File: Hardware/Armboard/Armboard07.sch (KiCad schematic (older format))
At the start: 30 parts

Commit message: Assigned R/L/C footprints
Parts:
- R24, R25, R26, R27, R28, R29, R30, R31, R32, R33: renamed from R?; footprint (none) -> Resistor_SMD:R_0603_1608Metric_Pad1.05x0.95mm_HandSolder
- gave numbers to parts that had none: 20

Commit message: Added more footprints
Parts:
- Conn14, Conn15, Conn16, Conn17: footprint (none) -> MRDT_Connectors:MOLEX_SL_02_Horizontal
- D18, D19, D20, D21, D22, D23, D24, D25, D26, D27: footprint (none) -> LED_SMD:LED_0603_1608Metric_Pad1.05x0.95mm_HandSolder
- SW1, SW2, SW3, SW4, SW5, SW6: footprint (none) -> Button_Switch_SMD:SW_Push_1P1T_NO_6x6mm_H9.5mm
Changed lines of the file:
@@
 F 0 "D24" V 6989 2892 50  0000 R CNN
 F 1 "LED" V 6898 2892 50  0000 R CNN
-F 2 "" H 6950 3010 50  0001 C CNN
+F 2 "LED_SMD:LED_0603_1608Metric_Pad1.05x0.95mm_HandSolder" H 6950 3010 50  0001 C CNN
 F 3 "~" H 6950 3010 50  0001 C CNN
 	1    6950 3010
@@
 F 0 "Conn14" H 7418 2618 60  0000 L CNN
 F 1 "Molex_SL_02" H 7418 2512 60  0000 L CNN
-F 2 "" H 7290 2360 60  0001 C CNN
+F 2 "MRDT_Connectors:MOLEX_SL_02_Horizontal" H 7290 2360 60  0001 C CNN
 F 3 "" H 7290 2360 60  0001 C CNN
 	1    7290 2460
@@
 F 0 "D25" V 6989 4792 50  0000 R CNN
 F 1 "LED" V 6898 4792 50  0000 R CNN
-F 2 "" H 6950 4910 50  0001 C CNN
+F 2 "LED_SMD:LED_0603_1608Metric_Pad1.05x0.95mm_HandSolder" H 6950 4910 50  0001 C CNN
 F 3 "~" H 6950 4910 50  0001 C CNN
 	1    6950 4910
@@
 F 0 "Conn15" H 7418 4518 60  0000 L CNN
 F 1 "Molex_SL_02" H 7418 4412 60  0000 L CNN
-F 2 "" H 7290 4260 60  0001 C CNN
+F 2 "MRDT_Connectors:MOLEX_SL_02_Horizontal" H 7290 4260 60  0001 C CNN
 F 3 "" H 7290 4260 60  0001 C CNN
 	1    7290 4360
@@
 F 0 "D26" V 8949 2922 50  0000 R CNN
 F 1 "LED" V 8858 2922 50  0000 R CNN
-F 2 "" H 8910 3040 50  0001 C CNN
+F 2 "LED_SMD:LED_0603_1608Metric_Pad1.05x0.95mm_HandSolder" H 8910 3040 50  0001 C CNN
 F 3 "~" H 8910 3040 50  0001 C CNN
 	1    8910 3040
@@
 F 0 "Conn16" H 9378 2648 60  0000 L CNN
 F 1 "Molex_SL_02" H 9378 2542 60  0000 L CNN
-F 2 "" H 9250 2390 60  0001 C CNN
+F 2 "MRDT_Connectors:MOLEX_SL_02_Horizontal" H 9250 2390 60  0001 C CNN
 F 3 "" H 9250 2390 60  0001 C CNN
 	1    9250 2490
@@
 F 0 "D27" V 8949 4822 50  0000 R CNN
 F 1 "LED" V 8858 4822 50  0000 R CNN
-F 2 "" H 8910 4940 50  0001 C CNN
+F 2 "LED_SMD:LED_0603_1608Metric_Pad1.05x0.95mm_HandSolder" H 8910 4940 50  0001 C CNN
 F 3 "~" H 8910 4940 50  0001 C CNN
 	1    8910 4940
@@
 F 0 "Conn17" H 9378 4548 60  0000 L CNN
 F 1 "Molex_SL_02" H 9378 4442 60  0000 L CNN
-F 2 "" H 9250 4290 60  0001 C CNN
+F 2 "MRDT_Connectors:MOLEX_SL_02_Horizontal" H 9250 4290 60  0001 C CNN
 F 3 "" H 9250 4290 60  0001 C CNN
 	1    9250 4390
@@
 F 0 "SW1" H 2550 2035 50  0000 C CNN
 F 1 "SW_Push" H 2550 1944 50  0000 C CNN
-F 2 "" H 2550 1950 50  0001 C CNN
+F 2 "Button_Switch_SMD:SW_Push_1P1T_NO_6x6mm_H9.5mm" H 2550 1950 50  0001 C CNN
 F 3 "~" H 2550 1950 50  0001 C CNN
 	1    2550 1750
@@
 F 0 "SW2" H 2550 2985 50  0000 C CNN
 F 1 "SW_Push" H 2550 2894 50  0000 C CNN
-F 2 "" H 2550 2900 50  0001 C CNN
+F 2 "Button_Switch_SMD:SW_Push_1P1T_NO_6x6mm_H9.5mm" H 2550 2900 50  0001 C CNN
 F 3 "~" H 2550 2900 50  0001 C CNN
 	1    2550 2700
@@
 F 0 "SW3" H 2550 3935 50  0000 C CNN
 F 1 "SW_Push" H 2550 3844 50  0000 C CNN
-F 2 "" H 2550 3850 50  0001 C CNN
+F 2 "Button_Switch_SMD:SW_Push_1P1T_NO_6x6mm_H9.5mm" H 2550 3850 50  0001 C CNN
 F 3 "~" H 2550 3850 50  0001 C CNN
 	1    2550 3650
@@
 F 0 "SW4" H 2550 4935 50  0000 C CNN
 F 1 "SW_Push" H 2550 4844 50  0000 C CNN
-F 2 "" H 2550 4850 50  0001 C CNN
+F 2 "Button_Switch_SMD:SW_Push_1P1T_NO_6x6mm_H9.5mm" H 2550 4850 50  0001 C CNN
 F 3 "~" H 2550 4850 50  0001 C CNN
 	1    2550 4650
@@
 F 0 "SW5" H 2550 5885 50  0000 C CNN
 F 1 "SW_Push" H 2550 5794 50  0000 C CNN
-F 2 "" H 2550 5800 50  0001 C CNN
+F 2 "Button_Switch_SMD:SW_Push_1P1T_NO_6x6mm_H9.5mm" H 2550 5800 50  0001 C CNN
 F 3 "~" H 2550 5800 50  0001 C CNN
 	1    2550 5600
@@
 F 0 "SW6" H 2550 6835 50  0000 C CNN
 F 1 "SW_Push" H 2550 6744 50  0000 C CNN
-F 2 "" H 2550 6750 50  0001 C CNN
+F 2 "Button_Switch_SMD:SW_Push_1P1T_NO_6x6mm_H9.5mm" H 2550 6750 50  0001 C CNN
 F 3 "~" H 2550 6750 50  0001 C CNN
 	1    2550 6550
@@
 F 0 "D18" H 3493 1495 50  0000 C CNN
 F 1 "LED" H 3493 1586 50  0000 C CNN
-F 2 "" H 3500 1750 50  0001 C CNN
+F 2 "LED_SMD:LED_0603_1608Metric_Pad1.05x0.95mm_HandSolder" H 3500 1750 50  0001 C CNN
 F 3 "~" H 3500 1750 50  0001 C CNN
 	1    3500 1750
@@
 F 0 "D19" H 3493 2445 50  0000 C CNN
 F 1 "LED" H 3493 2536 50  0000 C CNN
-F 2 "" H 3500 2700 50  0001 C CNN
+F 2 "LED_SMD:LED_0603_1608Metric_Pad1.05x0.95mm_HandSolder" H 3500 2700 50  0001 C CNN
 F 3 "~" H 3500 2700 50  0001 C CNN
 	1    3500 2700
@@
 F 0 "D20" H 3493 3395 50  0000 C CNN
 F 1 "LED" H 3493 3486 50  0000 C CNN
-F 2 "" H 3500 3650 50  0001 C CNN
+F 2 "LED_SMD:LED_0603_1608Metric_Pad1.05x0.95mm_HandSolder" H 3500 3650 50  0001 C CNN
 F 3 "~" H 3500 3650 50  0001 C CNN
 	1    3500 3650
@@
 F 0 "D21" H 3493 4395 50  0000 C CNN
 F 1 "LED" H 3493 4486 50  0000 C CNN
-F 2 "" H 3500 4650 50  0001 C CNN
+F 2 "LED_SMD:LED_0603_1608Metric_Pad1.05x0.95mm_HandSolder" H 3500 4650 50  0001 C CNN
 F 3 "~" H 3500 4650 50  0001 C CNN
 	1    3500 4650
@@
 F 0 "D22" H 3493 5345 50  0000 C CNN
 F 1 "LED" H 3493 5436 50  0000 C CNN
-F 2 "" H 3500 5600 50  0001 C CNN
+F 2 "LED_SMD:LED_0603_1608Metric_Pad1.05x0.95mm_HandSolder" H 3500 5600 50  0001 C CNN
 F 3 "~" H 3500 5600 50  0001 C CNN
 	1    3500 5600
@@
 F 0 "D23" H 3493 6295 50  0000 C CNN
 F 1 "LED" H 3493 6386 50  0000 C CNN
-F 2 "" H 3500 6550 50  0001 C CNN
+F 2 "LED_SMD:LED_0603_1608Metric_Pad1.05x0.95mm_HandSolder" H 3500 6550 50  0001 C CNN
 F 3 "~" H 3500 6550 50  0001 C CNN
 	1    3500 6550

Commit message: Imported footprints to layout
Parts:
- Conn14, Conn15, Conn16, Conn17: footprint MRDT_Connectors:MOLEX_SL_02_Horizontal -> MRDT_Connectors:MOLEX_SL_02_Vertical
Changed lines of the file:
@@
 F 0 "Conn14" H 7418 2618 60  0000 L CNN
 F 1 "Molex_SL_02" H 7418 2512 60  0000 L CNN
-F 2 "MRDT_Connectors:MOLEX_SL_02_Horizontal" H 7290 2360 60  0001 C CNN
+F 2 "MRDT_Connectors:MOLEX_SL_02_Vertical" H 7290 2360 60  0001 C CNN
 F 3 "" H 7290 2360 60  0001 C CNN
 	1    7290 2460
@@
 F 0 "Conn15" H 7418 4518 60  0000 L CNN
 F 1 "Molex_SL_02" H 7418 4412 60  0000 L CNN
-F 2 "MRDT_Connectors:MOLEX_SL_02_Horizontal" H 7290 4260 60  0001 C CNN
+F 2 "MRDT_Connectors:MOLEX_SL_02_Vertical" H 7290 4260 60  0001 C CNN
 F 3 "" H 7290 4260 60  0001 C CNN
 	1    7290 4360
@@
 F 0 "Conn16" H 9378 2648 60  0000 L CNN
 F 1 "Molex_SL_02" H 9378 2542 60  0000 L CNN
-F 2 "MRDT_Connectors:MOLEX_SL_02_Horizontal" H 9250 2390 60  0001 C CNN
+F 2 "MRDT_Connectors:MOLEX_SL_02_Vertical" H 9250 2390 60  0001 C CNN
 F 3 "" H 9250 2390 60  0001 C CNN
 	1    9250 2490
@@
 F 0 "Conn17" H 9378 4548 60  0000 L CNN
 F 1 "Molex_SL_02" H 9378 4442 60  0000 L CNN
-F 2 "MRDT_Connectors:MOLEX_SL_02_Horizontal" H 9250 4290 60  0001 C CNN
+F 2 "MRDT_Connectors:MOLEX_SL_02_Vertical" H 9250 4290 60  0001 C CNN
 F 3 "" H 9250 4290 60  0001 C CNN
 	1    9250 4390

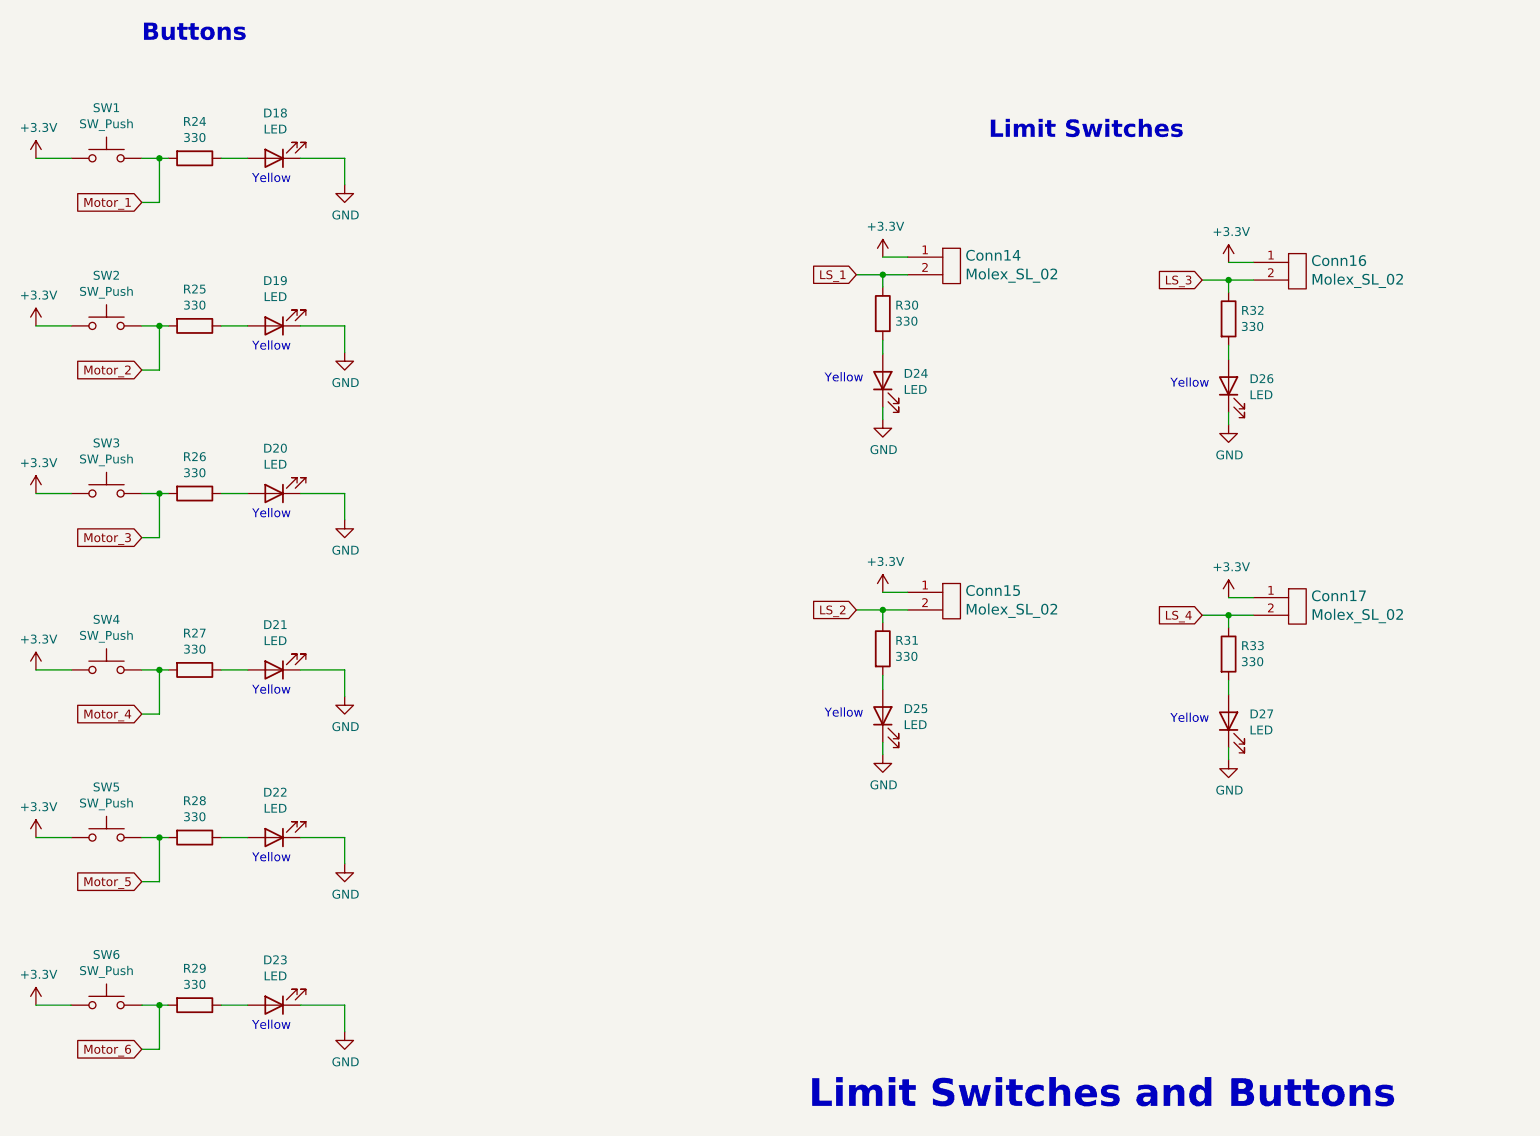
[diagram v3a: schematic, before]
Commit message: Double-checked schematic, pointed power pins up, made sure 12V and 3.3V were full networks
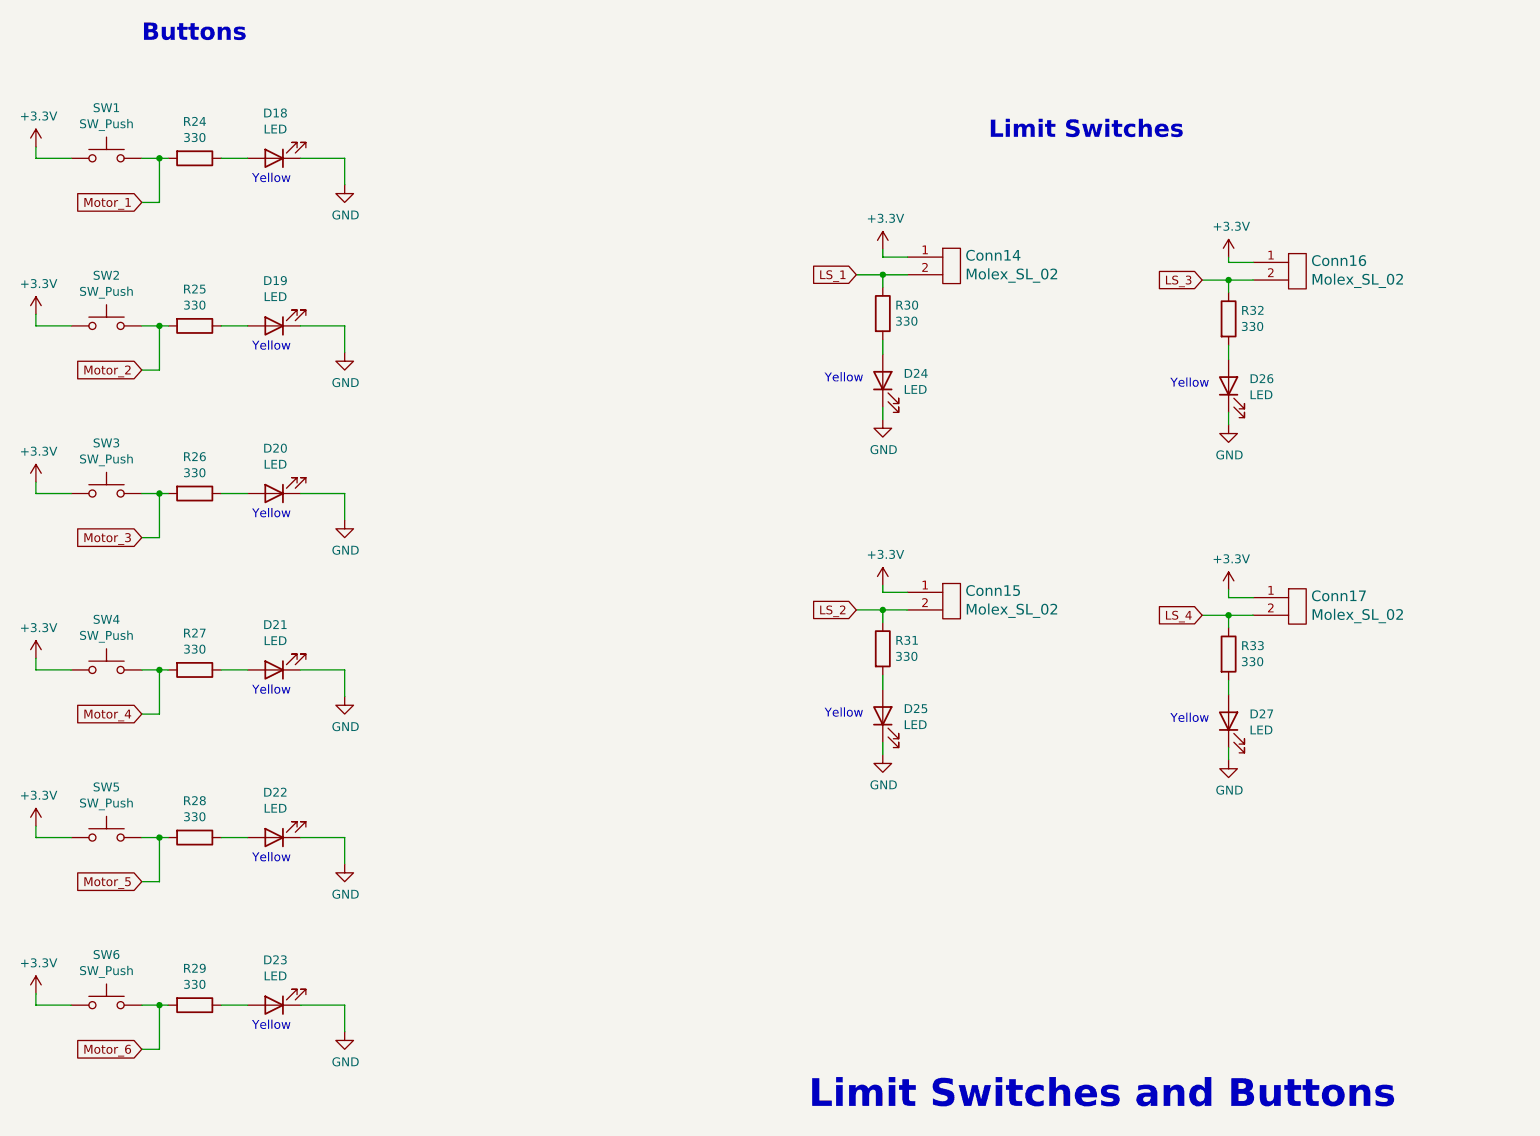
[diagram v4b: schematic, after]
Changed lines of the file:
@@
 L power:+3.3V #PWR041
 U 1 1 5F91F195
-P 2150 1750
-F 0 "#PWR041" H 2150 1600 50  0001 C CNN
-F 1 "+3.3V" H 2165 1923 50  0000 C CNN
-F 2 "" H 2150 1750 50  0001 C CNN
-F 3 "" H 2150 1750 50  0001 C CNN
-	1    2150 1750
+P 2150 1685
+F 0 "#PWR041" H 2150 1535 50  0001 C CNN
+F 1 "+3.3V" H 2165 1858 50  0000 C CNN
+F 2 "" H 2150 1685 50  0001 C CNN
+F 3 "" H 2150 1685 50  0001 C CNN
+	1    2150 1685
 	1    0    0    -1
 $EndComp
@@
 L power:+3.3V #PWR042
 U 1 1 5F923263
-P 2150 2700
-F 0 "#PWR042" H 2150 2550 50  0001 C CNN
-F 1 "+3.3V" H 2165 2873 50  0000 C CNN
-F 2 "" H 2150 2700 50  0001 C CNN
-F 3 "" H 2150 2700 50  0001 C CNN
-	1    2150 2700
+P 2150 2635
+F 0 "#PWR042" H 2150 2485 50  0001 C CNN
+F 1 "+3.3V" H 2165 2808 50  0000 C CNN
+F 2 "" H 2150 2635 50  0001 C CNN
+F 3 "" H 2150 2635 50  0001 C CNN
+	1    2150 2635
 	1    0    0    -1
 $EndComp
@@
 L power:+3.3V #PWR043
 U 1 1 5F924E57
-P 2150 3650
-F 0 "#PWR043" H 2150 3500 50  0001 C CNN
-F 1 "+3.3V" H 2165 3823 50  0000 C CNN
-F 2 "" H 2150 3650 50  0001 C CNN
-F 3 "" H 2150 3650 50  0001 C CNN
-	1    2150 3650
+P 2150 3585
+F 0 "#PWR043" H 2150 3435 50  0001 C CNN
+F 1 "+3.3V" H 2165 3758 50  0000 C CNN
+F 2 "" H 2150 3585 50  0001 C CNN
+F 3 "" H 2150 3585 50  0001 C CNN
+	1    2150 3585
 	1    0    0    -1
 $EndComp
@@
 L power:+3.3V #PWR044
 U 1 1 5F9269C5
-P 2150 4650
-F 0 "#PWR044" H 2150 4500 50  0001 C CNN
-F 1 "+3.3V" H 2165 4823 50  0000 C CNN
-F 2 "" H 2150 4650 50  0001 C CNN
-F 3 "" H 2150 4650 50  0001 C CNN
-	1    2150 4650
+P 2150 4585
+F 0 "#PWR044" H 2150 4435 50  0001 C CNN
+F 1 "+3.3V" H 2165 4758 50  0000 C CNN
+F 2 "" H 2150 4585 50  0001 C CNN
+F 3 "" H 2150 4585 50  0001 C CNN
+	1    2150 4585
 	1    0    0    -1
 $EndComp
@@
 L power:+3.3V #PWR045
 U 1 1 5F9284DA
-P 2150 5600
-F 0 "#PWR045" H 2150 5450 50  0001 C CNN
-F 1 "+3.3V" H 2165 5773 50  0000 C CNN
-F 2 "" H 2150 5600 50  0001 C CNN
-F 3 "" H 2150 5600 50  0001 C CNN
-	1    2150 5600
+P 2150 5535
+F 0 "#PWR045" H 2150 5385 50  0001 C CNN
+F 1 "+3.3V" H 2165 5708 50  0000 C CNN
+F 2 "" H 2150 5535 50  0001 C CNN
+F 3 "" H 2150 5535 50  0001 C CNN
+	1    2150 5535
 	1    0    0    -1
 $EndComp
@@
 L power:+3.3V #PWR046
 U 1 1 5F92A093
-P 2150 6550
-F 0 "#PWR046" H 2150 6400 50  0001 C CNN
-F 1 "+3.3V" H 2165 6723 50  0000 C CNN
-F 2 "" H 2150 6550 50  0001 C CNN
-F 3 "" H 2150 6550 50  0001 C CNN
-	1    2150 6550
+P 2150 6485
+F 0 "#PWR046" H 2150 6335 50  0001 C CNN
+F 1 "+3.3V" H 2165 6658 50  0000 C CNN
+F 2 "" H 2150 6485 50  0001 C CNN
+F 3 "" H 2150 6485 50  0001 C CNN
+	1    2150 6485
 	1    0    0    -1
 $EndComp
@@
 L power:+3.3V #PWR053
 U 1 1 5F932624
-P 6950 2310
-F 0 "#PWR053" H 6950 2160 50  0001 C CNN
-F 1 "+3.3V" H 6965 2483 50  0000 C CNN
-F 2 "" H 6950 2310 50  0001 C CNN
-F 3 "" H 6950 2310 50  0001 C CNN
-	1    6950 2310
+P 6950 2265
+F 0 "#PWR053" H 6950 2115 50  0001 C CNN
+F 1 "+3.3V" H 6965 2438 50  0000 C CNN
+F 2 "" H 6950 2265 50  0001 C CNN
+F 3 "" H 6950 2265 50  0001 C CNN
+	1    6950 2265
 	1    0    0    -1
 $EndComp
@@
 L power:+3.3V #PWR057
 U 1 1 5F934170
-P 8910 2340
-F 0 "#PWR057" H 8910 2190 50  0001 C CNN
-F 1 "+3.3V" H 8925 2513 50  0000 C CNN
-F 2 "" H 8910 2340 50  0001 C CNN
-F 3 "" H 8910 2340 50  0001 C CNN
-	1    8910 2340
+P 8910 2310
+F 0 "#PWR057" H 8910 2160 50  0001 C CNN
+F 1 "+3.3V" H 8925 2483 50  0000 C CNN
+F 2 "" H 8910 2310 50  0001 C CNN
+F 3 "" H 8910 2310 50  0001 C CNN
+	1    8910 2310
 	1    0    0    -1
 $EndComp
@@
 L power:+3.3V #PWR059
 U 1 1 5F935C61
-P 8910 4240
-F 0 "#PWR059" H 8910 4090 50  0001 C CNN
-F 1 "+3.3V" H 8925 4413 50  0000 C CNN
-F 2 "" H 8910 4240 50  0001 C CNN
-F 3 "" H 8910 4240 50  0001 C CNN
-	1    8910 4240
+P 8910 4195
+F 0 "#PWR059" H 8910 4045 50  0001 C CNN
+F 1 "+3.3V" H 8925 4368 50  0000 C CNN
+F 2 "" H 8910 4195 50  0001 C CNN
+F 3 "" H 8910 4195 50  0001 C CNN
+	1    8910 4195
 	1    0    0    -1
 $EndComp
@@
 L power:+3.3V #PWR055
 U 1 1 5F93ADAC
-P 6950 4210
-F 0 "#PWR055" H 6950 4060 50  0001 C CNN
-F 1 "+3.3V" H 6965 4383 50  0000 C CNN
-F 2 "" H 6950 4210 50  0001 C CNN
-F 3 "" H 6950 4210 50  0001 C CNN
-	1    6950 4210
+P 6950 4170
+F 0 "#PWR055" H 6950 4020 50  0001 C CNN
+F 1 "+3.3V" H 6965 4343 50  0000 C CNN
+F 2 "" H 6950 4170 50  0001 C CNN
+F 3 "" H 6950 4170 50  0001 C CNN
+	1    6950 4170
 	1    0    0    -1
 $EndComp
@@
 Text Notes 3375 6700 0    50   ~ 0
 Yellow
+Wire Wire Line
+	2150 1685 2150 1750
+Wire Wire Line
+	2150 2635 2150 2700
+Wire Wire Line
+	2150 3585 2150 3650
+Wire Wire Line
+	2150 4650 2150 4585
+Wire Wire Line
+	2150 5535 2150 5600
+Wire Wire Line
+	2150 6550 2150 6485
+Wire Wire Line
+	6950 2310 6950 2265
+Wire Wire Line
+	6950 4210 6950 4170
+Wire Wire Line
+	8910 4195 8910 4240
+Wire Wire Line
+	8910 2340 8910 2310
 $EndSCHEMATC
